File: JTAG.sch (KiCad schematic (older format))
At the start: 45 parts, among them J11 MOLEX_87831-1420, J14 GRPB052VWQP-RC, Q17 BSS138LT1G, Q5 BSS138LT1G, U10 NC7SZ66P5X, U7 NC7SZ66P5X, U8 SN74AVC2T245RSWR, U9 SN74AVC2T245RSWR

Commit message: Strip extraneous AMC_FMC_Carrier-PcbDoc-rescue and powerMG from symbol names
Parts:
- J11: symbol marble_misc:MOLEX_87831-1420-MOLEX-AMC_FMC_Carrier-PcbDoc-rescue -> marble_misc:MOLEX_87831-1420-MOLEX
- J14: symbol marble_misc:Conn_ARM_JTAG_SWD_10-Connector-AMC_FMC_Carrier-PcbDoc-rescue -> marble_misc:Conn_ARM_JTAG_SWD_10-Connector
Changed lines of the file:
@@
 	10050 4150 10500 4150
 $Comp
-L marble_misc:MOLEX_87831-1420-MOLEX-AMC_FMC_Carrier-PcbDoc-rescue J11
+L marble_misc:MOLEX_87831-1420-MOLEX J11
 U 1 1 5CB763C1
 P 4200 4700
@@
 MMC_TDI
 $Comp
-L marble_misc:Conn_ARM_JTAG_SWD_10-Connector-AMC_FMC_Carrier-PcbDoc-rescue J?
+L marble_misc:Conn_ARM_JTAG_SWD_10-Connector J?
 U 1 1 5E9BF6F9
 P 5550 4050

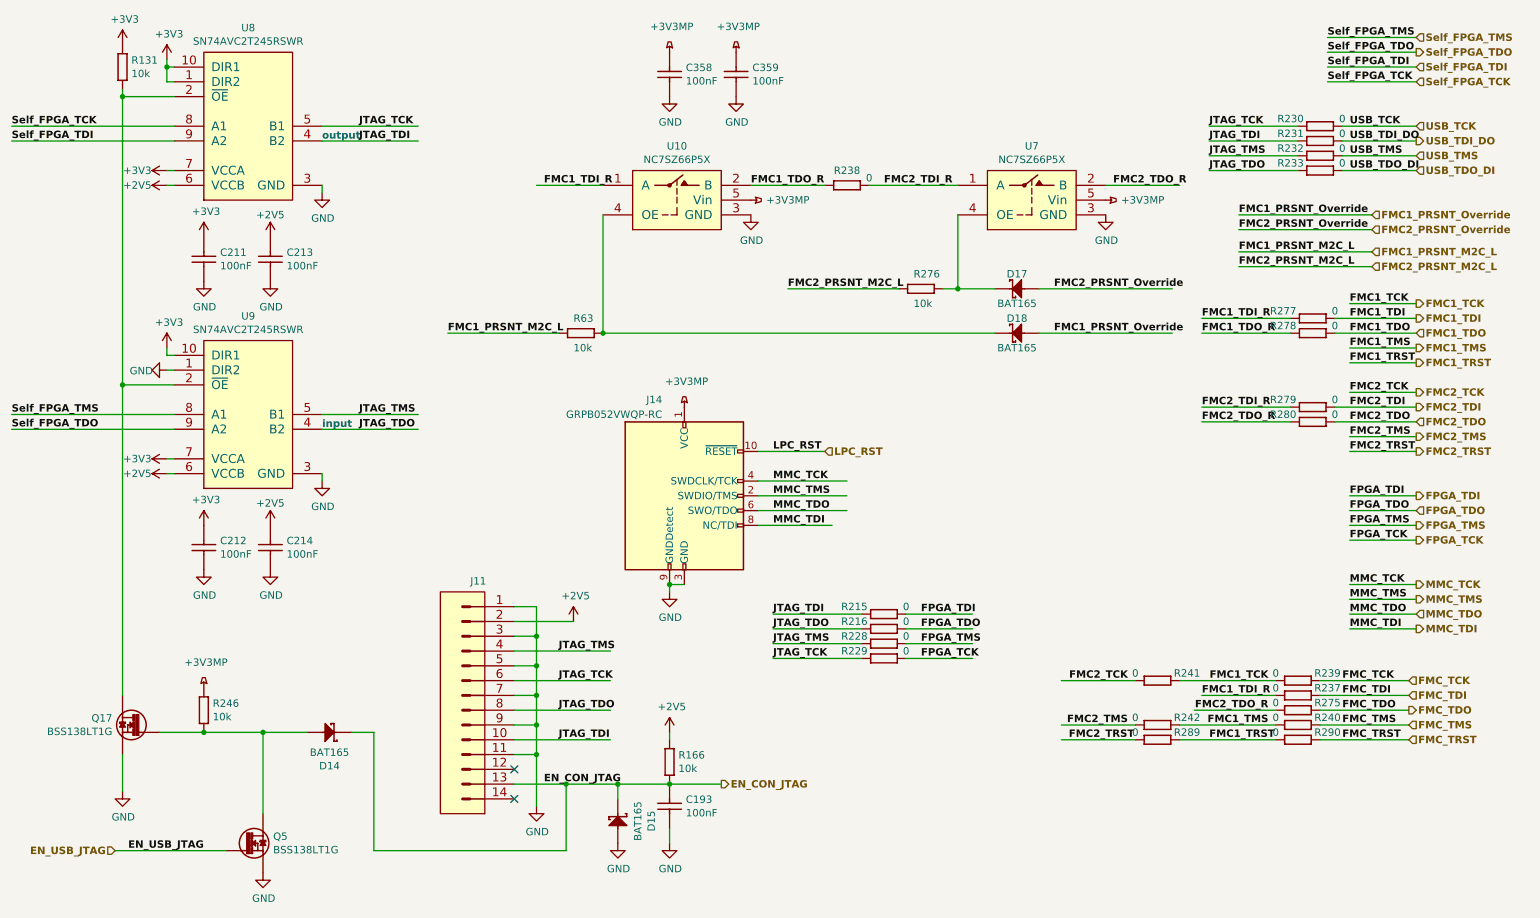
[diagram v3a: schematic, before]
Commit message: SCH: rename +3.3VP, 3V3PM and +3V3MP to +3V3P
  * all of them refer to the same net
  * to make confusion perfect, all 3 power symbols on the schematic
    were an instance of the symbol `+3.3VP` with different
    value attributes
  * renamed the `+3.3VP` symbol to `+3V3P` for naming consistency
  * SCH: replaced all power symbols on the net by the new one
  * PCB: still needs to be synced up, as the net name has changed
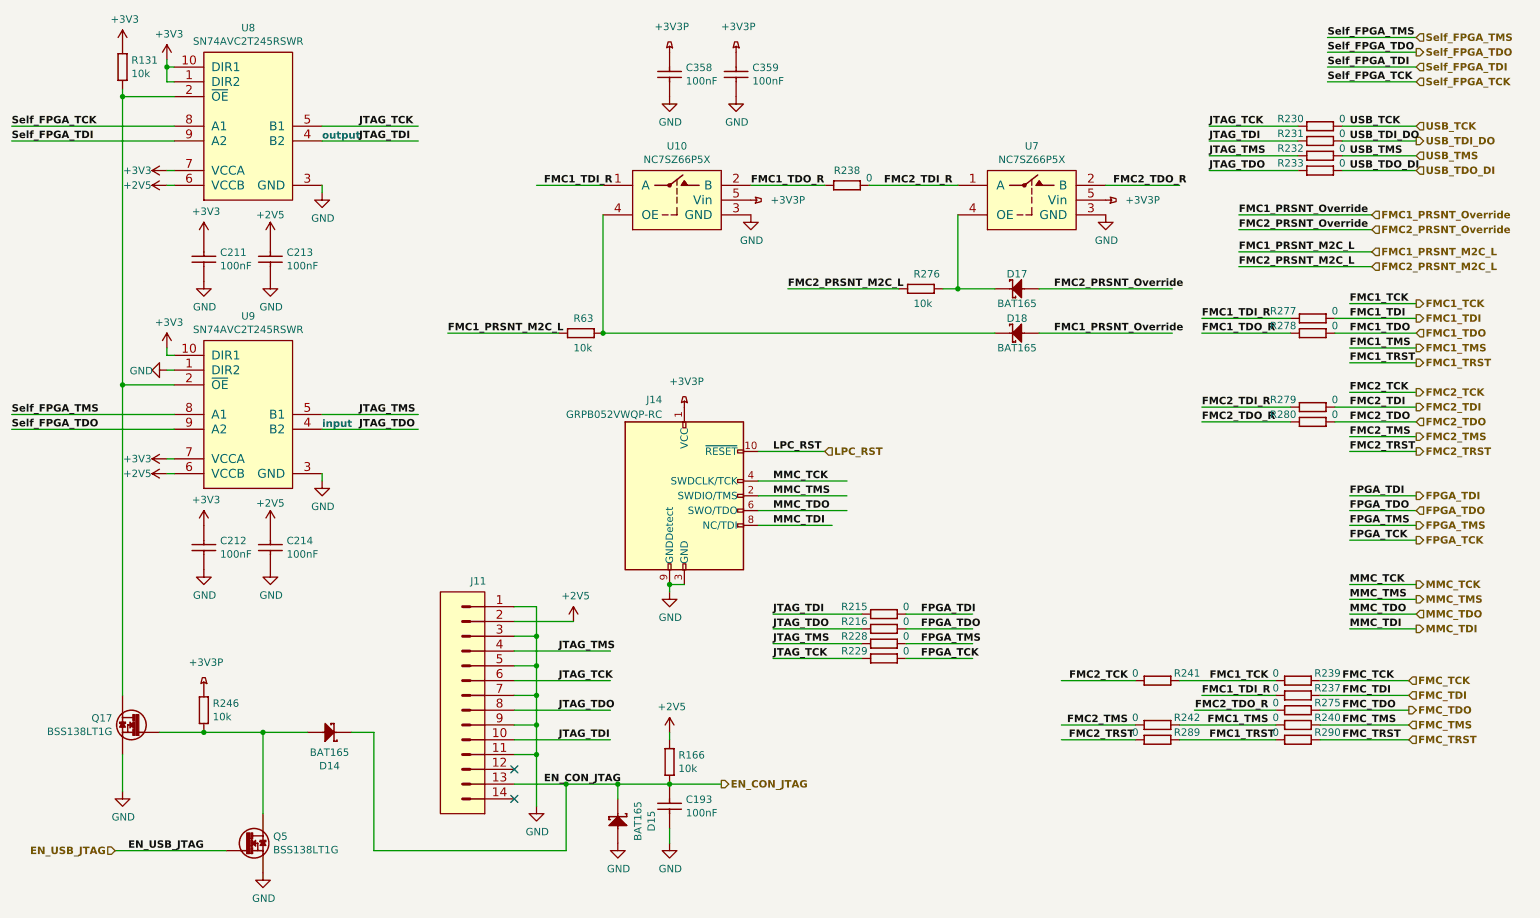
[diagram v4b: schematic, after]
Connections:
- net labels added: +3V3P
- net labels removed: +3V3MP
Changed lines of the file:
@@
 $EndComp
 $Comp
-L power:+3.3VP #PWR?
+L power:+3V3P #PWR?
 U 1 1 5D430167
 P 5450 1050
@@
 AR Path="/5D430167" Ref="#PWR0317"  Part="1"
 F 0 "#PWR0317" H 5450 900 50  0001 C CNN
-F 1 "+3V3MP" H 5465 1223 50  0000 C CNN
+F 1 "+3V3P" H 5465 1223 50  0000 C CNN
 F 2 "" H 5450 1050 50  0001 C CNN
 F 3 "" H 5450 1050 50  0001 C CNN
@@
 $EndComp
 $Comp
-L power:+3.3VP #PWR?
+L power:+3V3P #PWR?
 U 1 1 5D4357CC
 P 5900 1050
@@
 AR Path="/5D4357CC" Ref="#PWR0322"  Part="1"
 F 0 "#PWR0322" H 5900 900 50  0001 C CNN
-F 1 "+3V3MP" H 5915 1223 50  0000 C CNN
+F 1 "+3V3P" H 5915 1223 50  0000 C CNN
 F 2 "" H 5900 1050 50  0001 C CNN
 F 3 "" H 5900 1050 50  0001 C CNN
@@
 $EndComp
 $Comp
-L power:+3.3VP #PWR?
+L power:+3V3P #PWR?
 U 1 1 5D440498
 P 5550 3450
@@
 AR Path="/5D440498" Ref="#PWR0324"  Part="1"
 F 0 "#PWR0324" H 5550 3300 50  0001 C CNN
-F 1 "+3V3MP" H 5565 3623 50  0000 C CNN
+F 1 "+3V3P" H 5565 3623 50  0000 C CNN
 F 2 "" H 5550 3450 50  0001 C CNN
 F 3 "" H 5550 3450 50  0001 C CNN
@@
 $EndComp
 $Comp
-L power:+3.3VP #PWR?
+L power:+3V3P #PWR?
 U 1 1 5D445B1A
 P 6000 2050
@@
 AR Path="/5D445B1A" Ref="#PWR0589"  Part="1"
 F 0 "#PWR0589" H 6000 1900 50  0001 C CNN
-F 1 "+3V3MP" V 6000 2300 50  0000 C CNN
+F 1 "+3V3P" V 6000 2300 50  0000 C CNN
 F 2 "" H 6000 2050 50  0001 C CNN
 F 3 "" H 6000 2050 50  0001 C CNN
@@
 $EndComp
 $Comp
-L power:+3.3VP #PWR?
+L power:+3V3P #PWR?
 U 1 1 5D460C62
 P 8400 2050
@@
 AR Path="/5D460C62" Ref="#PWR0590"  Part="1"
 F 0 "#PWR0590" H 8400 1900 50  0001 C CNN
-F 1 "+3V3MP" V 8400 2300 50  0000 C CNN
+F 1 "+3V3P" V 8400 2300 50  0000 C CNN
 F 2 "" H 8400 2050 50  0001 C CNN
 F 3 "" H 8400 2050 50  0001 C CNN
@@
 $EndComp
 $Comp
-L power:+3.3VP #PWR?
+L power:+3V3P #PWR?
 U 1 1 5D46B90D
 P 2300 5350
@@
 AR Path="/5D46B90D" Ref="#PWR0609"  Part="1"
 F 0 "#PWR0609" H 2300 5200 50  0001 C CNN
-F 1 "+3V3MP" H 2315 5523 50  0000 C CNN
+F 1 "+3V3P" H 2315 5523 50  0000 C CNN
 F 2 "" H 2300 5350 50  0001 C CNN
 F 3 "" H 2300 5350 50  0001 C CNN

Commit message: Convert all footprints to use Marble nickname
Includes both .sch and .lib files
Includes both bare footprint names and those with CERN-like nicknames
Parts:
- C193, C211, C212, C213, C214, C358, C359: footprint CAPC0603X33N -> Marble:CAPC0603X33N
- D14, D15, D17, D18: footprint ICs And Semiconductors SMD:SOD2512X110N -> Marble:SOD2512X110N
- J11: footprint MOLEX THD:MOLEX_87831-1420 -> Marble:MOLEX_87831-1420
- J14: footprint Connector_PinHeader_1.27mm:PinHeader_2x05_P1.27mm_Vertical_SMD -> Marble:PinHeader_2x05_P1.27mm_Vertical_SMD
- Q17, Q5: footprint ICs And Semiconductors SMD:SOT95P240X110-3N -> Marble:SOT95P240X110-3N
- R131, R166, R215, R216, R228, R229, R230, R231, R232, R233, R237, R238, R239, R240, R241, R242, R246, R275, R276, R277, R278, R279, R280, R289, R290, R63: footprint RESC1005X40N -> Marble:RESC1005X40N
- U10, U7: footprint SOT65P210X110-5N -> Marble:SOT65P210X110-5N
- U8, U9: footprint ICs And Semiconductors SMD:QFN40P140X180X55-10N -> Marble:QFN40P140X180X55-10N

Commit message: Clean up BSS138 instances in schematic
Q5 Q6 Q8 Q9 Q14 Q17 Q18 Q19 Q20 Q21 Q24
Fewer warnings from KiBoM
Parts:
- Q17, Q5: HelpURL \\\\cern.ch\\dfs\\Applications\\Altium\\Datasheets\\BSS139.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 -> \\\\cern.ch\\dfs\\Applications\\Altium\\Datasheets\\BSS138L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
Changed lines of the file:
@@
 F 1 "BSS138LT1G" H 2319 5655 50  0000 L CNN
 F 2 "Marble:SOT95P240X110-3N" H 2000 4440 60  0001 L CNN
-F 3 "\\\\cern.ch\\dfs\\Applications\\Altium\\Datasheets\\BSS139.pdf" H 2000 5160 60  0001 L CNN
+F 3 "\\\\cern.ch\\dfs\\Applications\\Altium\\Datasheets\\BSS138LT1G.pdf" H 2000 5160 60  0001 L CNN
 F 4 "BSS138LT1G" H 2000 5070 60  0001 L CNN "Part Number"
 F 5 "N-MOSFET-D 1G 2S 3D" H 2000 4980 60  0001 L CNN "Library Ref"
@@
 F 27 "PcbLib\\ICs And Semiconductors SMD.PcbLib" H 2000 2910 60  0001 L CNN "Footprint Path"
 F 28 "SOT95P240X110-3N" H 2000 2820 60  0001 L CNN "Footprint Ref"
-F 29 "\\\\cern.ch\\dfs\\Applications\\Altium\\Datasheets\\BSS139.pdf" H 2000 2730 60  0001 L CNN "HelpURL"
+F 29 "\\\\cern.ch\\dfs\\Applications\\Altium\\Datasheets\\BSS138LT1G.pdf" H 2000 2730 60  0001 L CNN "HelpURL"
 F 30 "~~" H 2000 2640 60  0001 L CNN "ComponentLink1URL"
 F 31 " " H 2000 2550 60  0001 L CNN "ComponentLink1Description"
@@
 F 1 "BSS138LT1G" H 2769 6455 50  0000 L CNN
 F 2 "Marble:SOT95P240X110-3N" H 2450 5240 60  0001 L CNN
-F 3 "\\\\cern.ch\\dfs\\Applications\\Altium\\Datasheets\\BSS139.pdf" H 2450 5960 60  0001 L CNN
+F 3 "\\\\cern.ch\\dfs\\Applications\\Altium\\Datasheets\\BSS138LT1G.pdf" H 2450 5960 60  0001 L CNN
 F 4 "BSS138LT1G" H 2450 5870 60  0001 L CNN "Part Number"
 F 5 "N-MOSFET-D 1G 2S 3D" H 2450 5780 60  0001 L CNN "Library Ref"
@@
 F 27 "PcbLib\\ICs And Semiconductors SMD.PcbLib" H 2450 3710 60  0001 L CNN "Footprint Path"
 F 28 "SOT95P240X110-3N" H 2450 3620 60  0001 L CNN "Footprint Ref"
-F 29 "\\\\cern.ch\\dfs\\Applications\\Altium\\Datasheets\\BSS139.pdf" H 2450 3530 60  0001 L CNN "HelpURL"
+F 29 "\\\\cern.ch\\dfs\\Applications\\Altium\\Datasheets\\BSS138LT1G.pdf" H 2450 3530 60  0001 L CNN "HelpURL"
 F 30 "~~" H 2450 3440 60  0001 L CNN "ComponentLink1URL"
 F 31 " " H 2450 3350 60  0001 L CNN "ComponentLink1Description"

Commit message: Get rid of most .DbLib suffixes in Library Name attributes
Enough that KiBoM no longer complains about them
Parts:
- Q17, Q5: Library Name ICs And Semiconductors.DbLib -> ICs And Semiconductors SMD
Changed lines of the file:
@@
 F 35 "03/23/09 00:00:00" H 2000 2190 60  0001 L CNN "CreateDate"
 F 36 "03/23/09 00:00:00" H 2000 2100 60  0001 L CNN "LatestRevisionDate"
-F 37 "ICs And Semiconductors.DbLib" H 2000 2010 60  0001 L CNN "Library Name"
+F 37 "ICs And Semiconductors SMD" H 2000 2010 60  0001 L CNN "Library Name"
 F 38 "This work is licensed under the Creative Commons CC-BY-SA 4.0 License. To the extent that circuit schematics that use Licensed Material can be considered to be ‘Adapted Material’, then the copyright holder waives article 3.b of the license with respect to these schematics." H 2000 1920 60  0001 L CNN "License"
 F 39 "Transistors" H 2000 5650 50  0001 C CNN "Database Table Name"
@@
 F 35 "03/23/09 00:00:00" H 2450 2990 60  0001 L CNN "CreateDate"
 F 36 "03/23/09 00:00:00" H 2450 2900 60  0001 L CNN "LatestRevisionDate"
-F 37 "ICs And Semiconductors.DbLib" H 2450 2810 60  0001 L CNN "Library Name"
+F 37 "ICs And Semiconductors SMD" H 2450 2810 60  0001 L CNN "Library Name"
 F 38 "This work is licensed under the Creative Commons CC-BY-SA 4.0 License. To the extent that circuit schematics that use Licensed Material can be considered to be ‘Adapted Material’, then the copyright holder waives article 3.b of the license with respect to these schematics." H 2450 2720 60  0001 L CNN "License"
 F 39 "Transistors" H 2450 6450 50  0001 C CNN "Database Table Name"

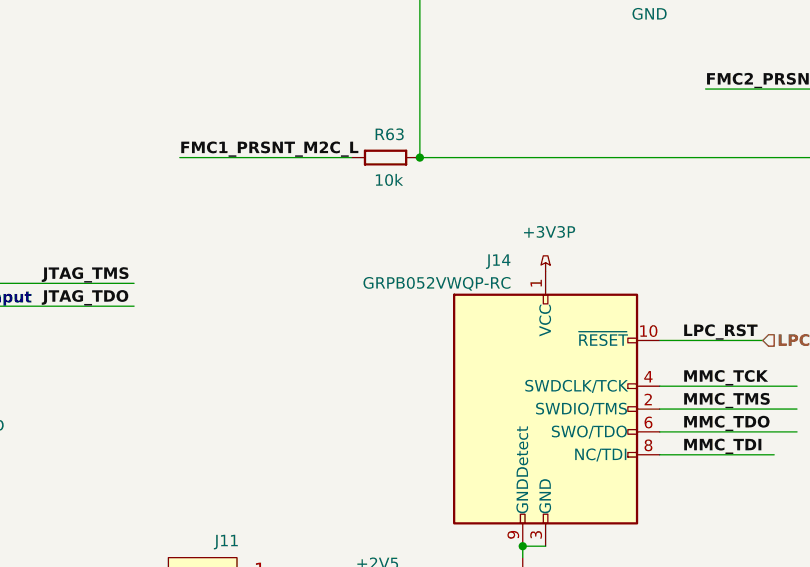
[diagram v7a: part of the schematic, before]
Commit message: replaced J14 connector, TCA9517 added, Exar chip hex files added
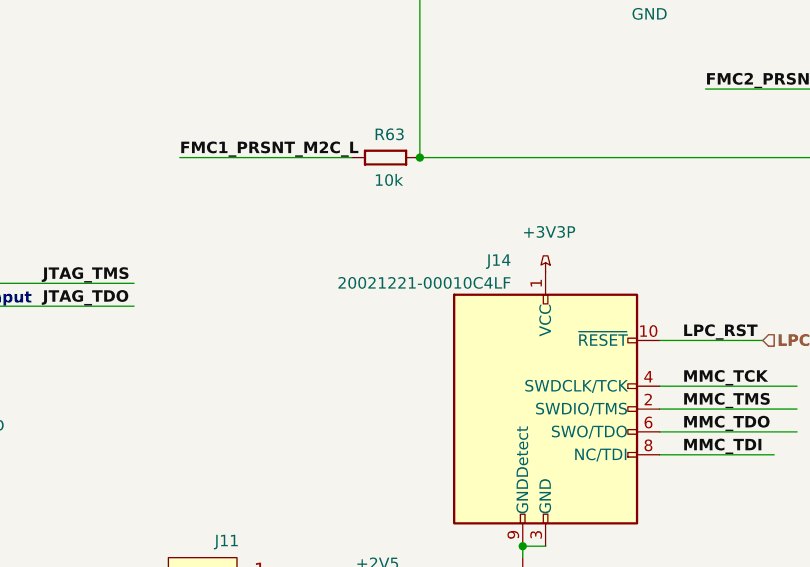
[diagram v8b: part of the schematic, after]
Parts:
- J14: value GRPB052VWQP-RC -> 20021221-00010C4LF; footprint Marble:PinHeader_2x05_P1.27mm_Vertical_SMD -> Marble:20021221-00010C4LF; Manufacturer Part Number GRPB052VWQP-RC -> 20021221-00010C4LF
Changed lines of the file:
@@
 AR Path="/5CA40231/5E9BF6F9" Ref="J14"  Part="1"
 F 0 "J14" H 5400 4700 50  0000 R CNN
-F 1 "GRPB052VWQP-RC" H 5400 4600 50  0000 R CNN
-F 2 "Marble:PinHeader_2x05_P1.27mm_Vertical_SMD" H 5600 3500 50  0001 L TNN
+F 1 "20021221-00010C4LF" H 5400 4600 50  0000 R CNN
+F 2 "Marble:20021221-00010C4LF" H 5600 3500 50  0001 L TNN
 F 3 "http://infocenter.arm.com/help/topic/com.arm.doc.faqs/attached/13634/cortex_debug_connectors.pdf" V 5200 2800 50  0001 C CNN
-F 4 "GRPB052VWQP-RC" H 5550 4050 50  0001 C CNN "Manufacturer Part Number"
+F 4 "20021221-00010C4LF" H 5550 4050 50  0001 C CNN "Manufacturer Part Number"
 	1    5550 4050
 	1    0    0    -1
